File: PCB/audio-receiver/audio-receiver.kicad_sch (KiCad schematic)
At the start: 5 parts, among them J1 Screw_Terminal_01x03, J2 Conn_01x04_Socket, J3 Screw_Terminal_01x02

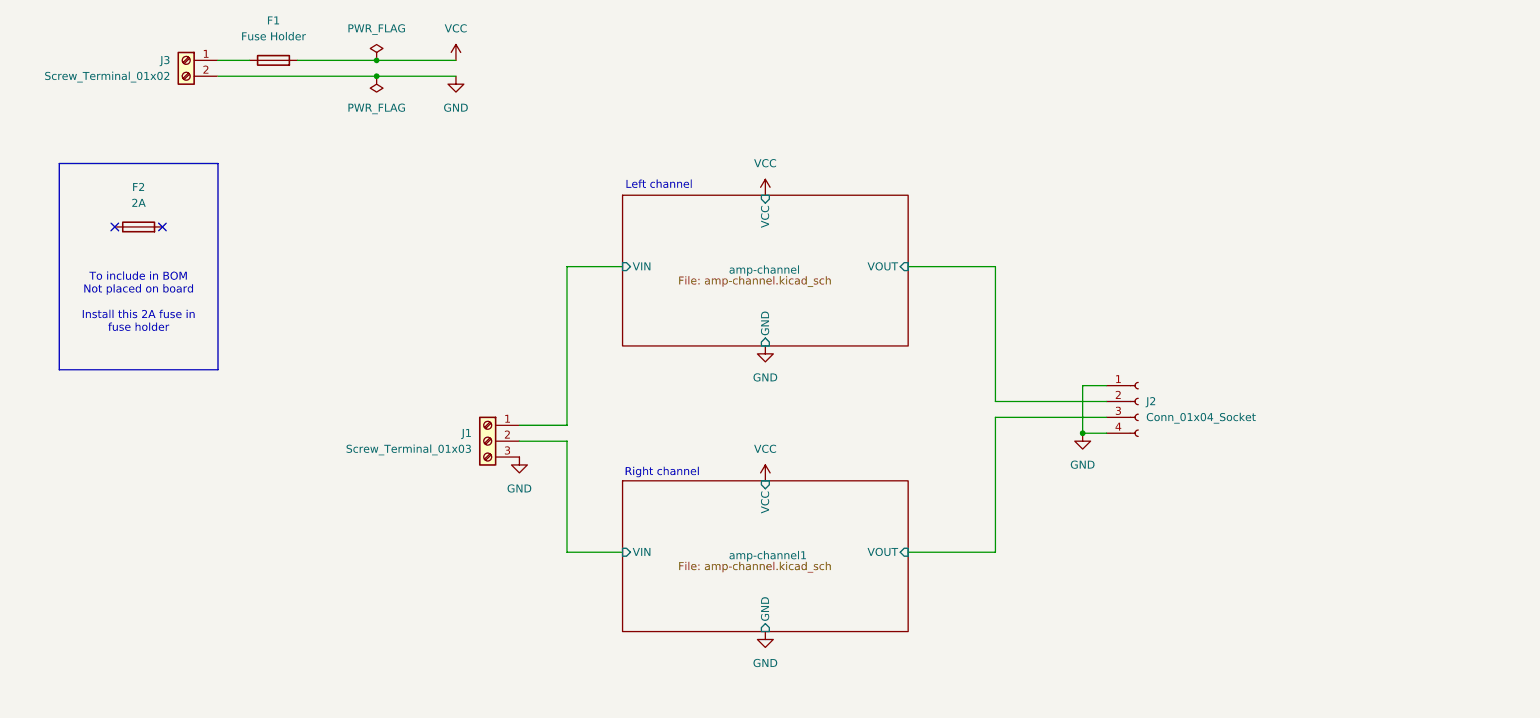
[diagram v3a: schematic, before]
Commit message: add bom, edit symbols, assign some footprints
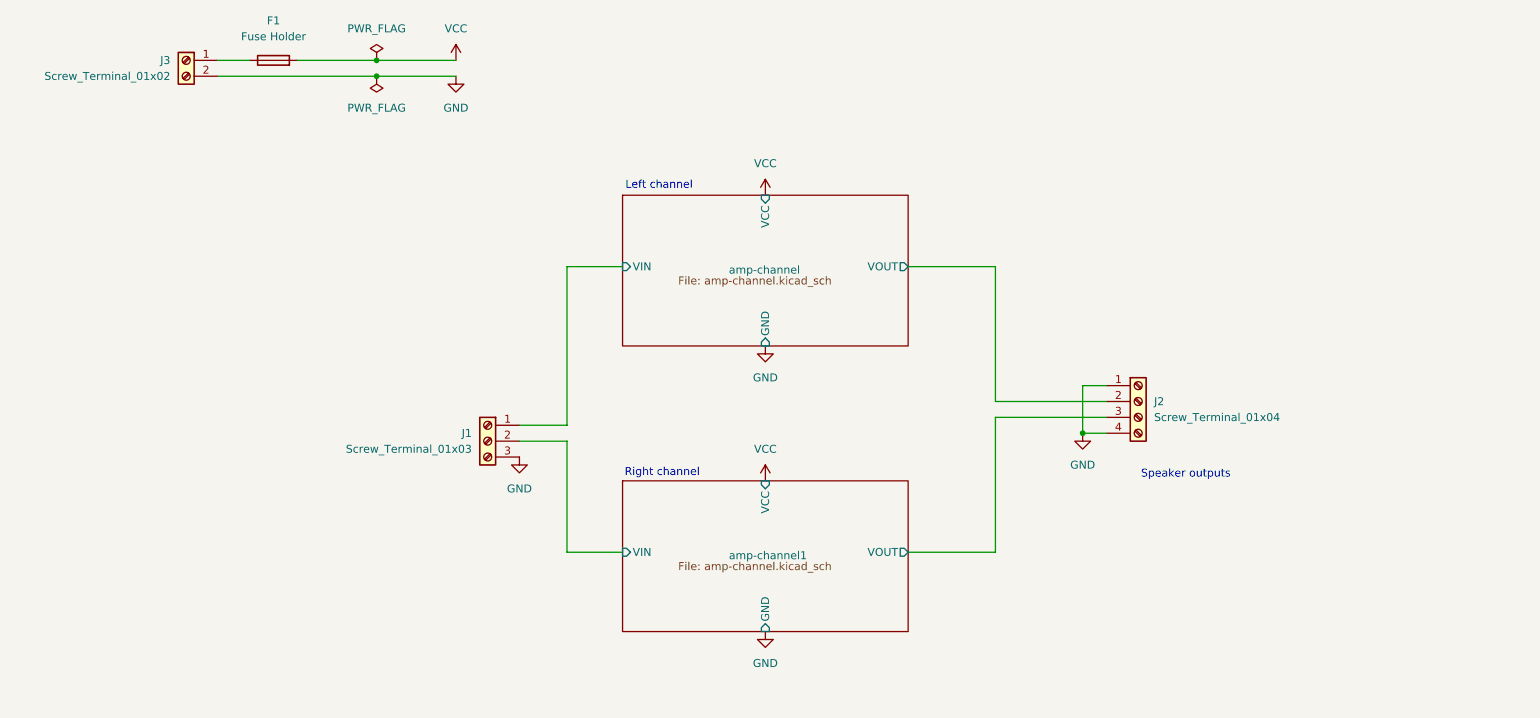
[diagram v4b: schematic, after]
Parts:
- removed F2: 2A, symbol Device:Fuse
- removed J2: Conn_01x04_Socket, symbol Connector:Conn_01x04_Socket
- added J2: Screw_Terminal_01x04, TerminalBlock_CUI:TerminalBlock_CUI_TB007-508-04_1x04_P5.08mm_Horizontal, symbol Connector:Screw_Terminal_01x04
- F1: Mouser PN (none) -> 504-1A5601
- J1: footprint (none) -> Connector_Phoenix_MSTB:PhoenixContact_MSTBA_2,5_3-G-5,08_1x03_P5.08mm_Horizontal; Mouser PN (none) -> 651-1757255; Mouser URL (none) -> https://www.mouser.com/ProductDetail/Phoenix-Contact/175725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
- J3: footprint (none) -> TerminalBlock_CUI:TerminalBlock_CUI_TB007-508-02_1x02_P5.08mm_Horizontal; Mouser PN (none) -> 490-TB007-508-02BE; Mouser URL (none) -> https://www.mouser.com/ProductDetail/Same-Sky/TB007-508-02B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
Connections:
- net GND: now also J2.1 (Pin_1), J2.4 (Pin_4)
- net amp-channel/VOUT: now also J2.2 (Pin_2)
- net amp-channel1/VOUT: now also J2.3 (Pin_3)
- no-connect marks 2 -> 0
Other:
- note added: "Speaker outputs"
- note removed: "To include in BOM Not placed on board Install this 2A fuse in fuse holder"
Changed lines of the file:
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@@
 	(generator_version "9.0")
 	(paper "A4")
-	(rectangle
-		(start 25.4 49.53)
-		(end 50.8 82.55)
-		(stroke
-			(width 0)
-			(type default)
-		)
-		(fill
-			(type none)
-		)
-	)
-	(text "To include in BOM\nNot placed on board\n\nInstall this 2A fuse in\nfuse holder"
-		(exclude_from_sim no)
-		(at 38.1 71.882 0)
-		(effects
-			(font
-				(size 1.27 1.27)
-			)
-		)
-	)
 	(text "Left channel"
 		(exclude_from_sim no)
@@
 		)
 	)
+	(text "Speaker outputs"
+		(exclude_from_sim no)
+		(at 205.74 99.314 0)
+		(effects
+			(font
+				(size 1.27 1.27)
+			)
+		)
+	)
 	(text "Right channel"
 		(exclude_from_sim no)
@@
 		(color 0 0 0 0)
 	)
-	(no_connect
-		(at 41.91 59.69)
-	)
-	(no_connect
-		(at 34.29 59.69)
-	)
 	(wire
 		(pts
@@
 			)
 		)
+		(property "Mouser PN" "504-1A5601 "
+			(at 59.69 33.02 90)
+			(effects
+				(font
+					(size 1.27 1.27)
+				)
+				(hide yes)
+			)
+		)
 		(pin "2"
 		)
@@
 	)
 	(symbol
-		(lib_id "Device:Fuse")
-		(at 38.1 59.69 90)
-		(unit 1)
-		(exclude_from_sim no)
-		(in_bom yes)
-		(on_board no)
-		(dnp no)
-		(fields_autoplaced yes)
-		(property "Reference" "F2"
-			(at 38.1 53.34 90)
-			(effects
-				(font
-					(size 1.27 1.27)
-				)
-			)
-		)
-		(property "Value" "2A"
-			(at 38.1 55.88 90)
-			(effects
-				(font
-					(size 1.27 1.27)
-				)
-			)
-		)
-		(property "Footprint" ""
-			(at 38.1 61.468 90)
-			(effects
-				(font
-					(size 1.27 1.27)
-				)
-				(hide yes)
-			)
-		)
-		(property "Datasheet" "https://www.mouser.com/datasheet/2/87/eaton_s500_glass_tube_fuses_data_sheet-1608830.pdf"
-			(at 38.1 59.69 0)
-			(effects
-				(font
-					(size 1.27 1.27)
-				)
-				(hide yes)
-			)
-		)
-		(property "Description" "Fuse"
-			(at 38.1 59.69 0)
-			(effects
-				(font
-					(size 1.27 1.27)
-				)
-				(hide yes)
-			)
-		)
-		(property "Mouser URL" "https://www.mouser.com/ProductDetail/Eaton-Electronics/BK1-S500-2-R?qs=9GX7soZQXxEC5%2FbW3phE%252Bg%3D%3D"
-			(at 38.1 59.69 90)
-			(effects
-				(font
-					(size 1.27 1.27)
-				)
-				(hide yes)
-			)
-		)
-		(pin "2"
-		)
-		(pin "1"
-		)
-		(instances
-			(project "audio-receiver"
-				(path "/c5a9eefd-b86f-4174-bbc7-e8261656b786"
-					(reference "F2")
-					(unit 1)
-				)
-			)
-		)
-	)
-	(symbol
 		(lib_id "power:VCC")
 		(at 138.43 54.61 0)
@@
 				(path "/c5a9eefd-b86f-4174-bbc7-e8261656b786"
 					(reference "#PWR016")
-					(unit 1)
-				)
-			)
-		)
-	)
-	(symbol
-		(lib_id "Connector:Conn_01x04_Socket")
-		(at 198.12 87.63 0)
-		(unit 1)
-		(exclude_from_sim no)
-		(in_bom yes)
-		(on_board yes)
-		(dnp no)
-		(fields_autoplaced yes)
-		(property "Reference" "J2"
-			(at 199.39 87.6299 0)
-			(effects
-				(font
-					(size 1.27 1.27)
-				)
-				(justify left)
-			)
-		)
-		(property "Value" "Conn_01x04_Socket"
-			(at 199.39 90.1699 0)
-			(effects
-				(font
-					(size 1.27 1.27)
-				)
-				(justify left)
-			)
-		)
-		(property "Footprint" ""
-			(at 198.12 87.63 0)
-			(effects
-				(font
-					(size 1.27 1.27)
-				)
-				(hide yes)
-			)
-		)
-		(property "Datasheet" ""
-			(at 198.12 87.63 0)
-			(effects
-				(font
-					(size 1.27 1.27)
-				)
-				(hide yes)
-			)
-		)
-		(property "Description" "Generic connector, single row, 01x04, script generated"
-			(at 198.12 87.63 0)
-			(effects
-				(font
-					(size 1.27 1.27)
-				)
-				(hide yes)
-			)
-		)
-		(property "Mouser URL" ""
-			(at 198.12 87.63 0)
-			(effects
-				(font
-					(size 1.27 1.27)
-				)
-				(hide yes)
-			)
-		)
-		(pin "4"
-		)
-		(pin "3"
-		)
-		(pin "1"
-		)
-		(pin "2"
-		)
-		(instances
-			(project ""
-				(path "/c5a9eefd-b86f-4174-bbc7-e8261656b786"
-					(reference "J2")
 					(unit 1)
 				)
@@
 			)
 		)
-		(property "Footprint" ""
+		(property "Footprint" "Connector_Phoenix_MSTB:PhoenixContact_MSTBA_2,5_3-G-5,08_1x03_P5.08mm_Horizontal"
 			(at 93.98 93.98 0)
 			(effects
@@
 			)
 		)
-		(property "Datasheet" ""
+		(property "Datasheet" "https://www.phoenixcontact.com/en-us/products/pcb-header-mstba-25-3-g-508-1757255?type=pdf"
 			(at 93.98 93.98 0)
 			(effects
@@
 			)
 		)
-		(property "Mouser URL" ""
+		(property "Mouser URL" "https://www.mouser.com/ProductDetail/Phoenix-Contact/1757255?qs=uD%2FdkN7XIa0ez8xszzicKg%3D%3D"
+			(at 93.98 93.98 0)
+			(effects
+				(font
+					(size 1.27 1.27)
+				)
+				(hide yes)
+			)
+		)
+		(property "Mouser PN" "651-1757255 "
 			(at 93.98 93.98 0)
 			(effects
@@
 				(path "/c5a9eefd-b86f-4174-bbc7-e8261656b786"
 					(reference "#PWR015")
+					(unit 1)
+				)
+			)
+		)
+	)
+	(symbol
+		(lib_id "Connector:Screw_Terminal_01x04")
+		(at 198.12 87.63 0)
+		(unit 1)
+		(exclude_from_sim no)
+		(in_bom yes)
+		(on_board yes)
+		(dnp no)
+		(fields_autoplaced yes)
+		(property "Reference" "J2"
+			(at 200.66 87.6299 0)
+			(effects
+				(font
+					(size 1.27 1.27)
+				)
+				(justify left)
+			)
+		)
+		(property "Value" "Screw_Terminal_01x04"
+			(at 200.66 90.1699 0)
+			(effects
+				(font
+					(size 1.27 1.27)
+				)
+				(justify left)
+			)
+		)
+		(property "Footprint" "TerminalBlock_CUI:TerminalBlock_CUI_TB007-508-04_1x04_P5.08mm_Horizontal"
+			(at 198.12 87.63 0)
+			(effects
+				(font
+					(size 1.27 1.27)
+				)
+				(hide yes)
+			)
+		)
+		(property "Datasheet" "https://www.mouser.com/datasheet/2/1628/tb007_508-3511020.pdf"
+			(at 198.12 87.63 0)
+			(effects
+				(font
+					(size 1.27 1.27)
+				)
+				(hide yes)
+			)
+		)
+		(property "Description" "Generic screw terminal, single row, 01x04, script generated (kicad-library-utils/schlib/autogen/connector/)"
+			(at 198.12 87.63 0)
+			(effects
+				(font
+					(size 1.27 1.27)
+				)
+				(hide yes)
+			)
+		)
+		(property "Mouser URL" "https://www.mouser.com/ProductDetail/Same-Sky/TB007-508-04BE?qs=vLWxofP3U2wnrmN2C1kFLw%3D%3D"
+			(at 198.12 87.63 0)
+			(effects
+				(font
+					(size 1.27 1.27)
+				)
+				(hide yes)
+			)
+		)
+		(property "Mouser PN" "490-TB007-508-04BE "
+			(at 198.12 87.63 0)
+			(effects
+				(font
+					(size 1.27 1.27)
+				)
+				(hide yes)
+			)
+		)
+		(pin "2"
+		)
+		(pin "1"
+		)
+		(pin "4"
+		)
+		(pin "3"
+		)
+		(instances
+			(project ""
+				(path "/c5a9eefd-b86f-4174-bbc7-e8261656b786"
+					(reference "J2")
 					(unit 1)
 				)
@@
 			)
 		)
-		(property "Footprint" ""
+		(property "Footprint" "TerminalBlock_CUI:TerminalBlock_CUI_TB007-508-02_1x02_P5.08mm_Horizontal"
 			(at 45.72 33.02 0)
 			(effects
@@
 			)
 		)
-		(property "Datasheet" ""
+		(property "Datasheet" "https://www.cuidevices.com/product/resource/tb007-508.pdf"
 			(at 45.72 33.02 0)
 			(effects
@@
 			)
 		)
-		(property "Mouser URL" ""
+		(property "Mouser URL" "https://www.mouser.com/ProductDetail/Same-Sky/TB007-508-02BE?qs=vLWxofP3U2y6PFKAfCqKUQ%3D%3D"
+			(at 45.72 33.02 0)
+			(effects
+				(font
+					(size 1.27 1.27)
+				)
+				(hide yes)
+			)
+		)
+		(property "Mouser PN" "490-TB007-508-02BE "
 			(at 45.72 33.02 0)
 			(effects
@@
 			)
 		)
-		(pin "VOUT" input
+		(pin "VOUT" output
 			(at 161.29 111.76 0)
 			(effects
@@
 			)
 		)
-		(pin "VOUT" input
+		(pin "VOUT" output
 			(at 161.29 66.04 0)
 			(effects
